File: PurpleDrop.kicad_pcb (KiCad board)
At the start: 4 copper layers, 161 x 92 mm, 156 parts, among them J1 Conn_02x32_Odd_Even, J10 current shunt, J2 Conn_02x32_Odd_Even, J3 Conn_02x20_Odd_Even, J4 Conn_01x04, J5 Conn_01x04, J6 Conn_01x04, J7 Conn_02x04_Odd_Even, J8 Conn_02x10_Odd_Even, J9 Barrel_Jack_Switch, Q1 SSM3K329R, Q2 SSM3K329R, Q3 SSM3K329R, Q4 SSM3K329R, SW1 SW_SPDT, U1 HV507, U10 TL7702B, U11 LR8N8-G, U2 HV507, U3 74LVC2T45DCT, U4 74LVC2T45DCT, U5 74LVC2T45DCT, U6 MAX31865AA, U7 MAX31865AA, U8 PCA9685PW, U9 MAX31865AA

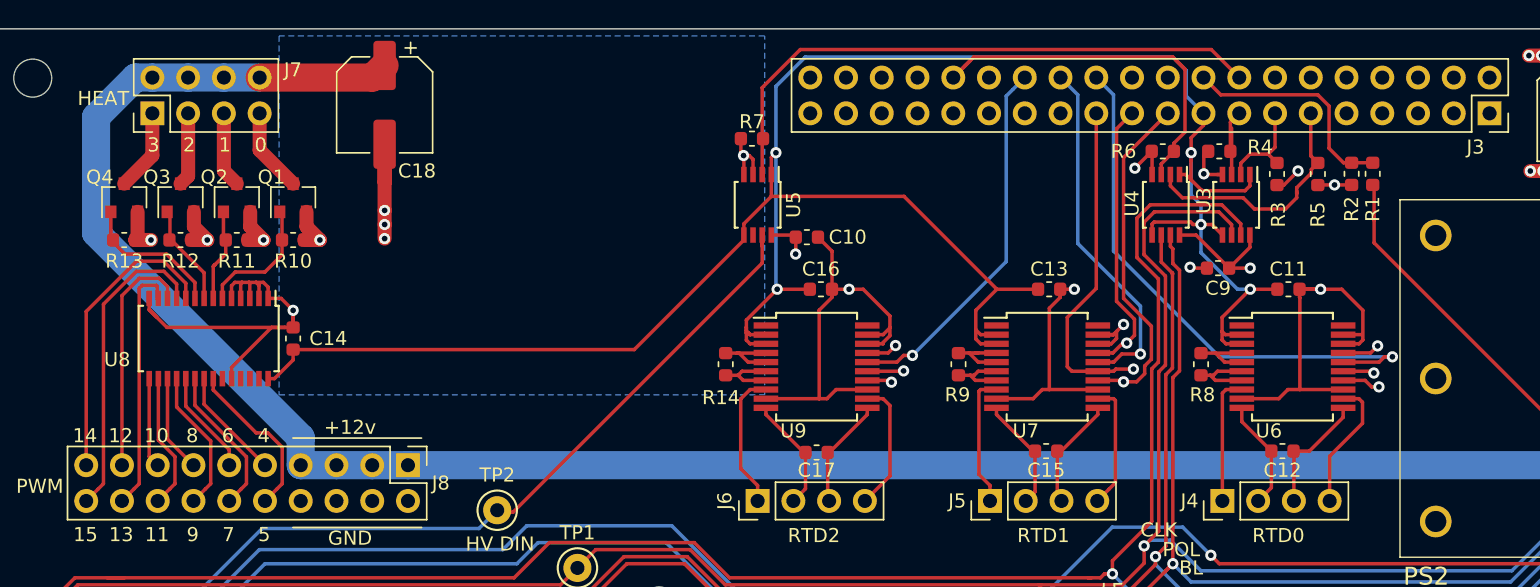
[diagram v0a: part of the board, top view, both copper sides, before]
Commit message: fixed missing i2c traces.  moved inner traces for SPI to back side
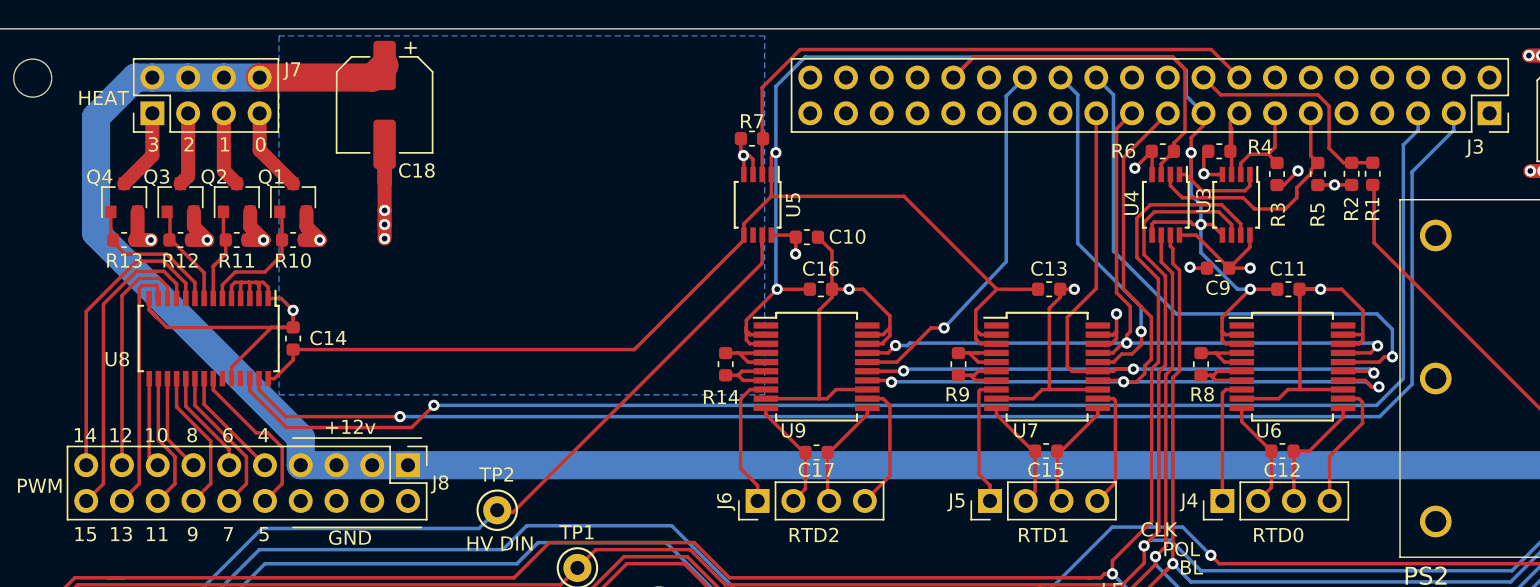
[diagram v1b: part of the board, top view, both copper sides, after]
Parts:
- renumbered He to H4
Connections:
- J3 pad 1: Net-(J3-Pad1) -> (no net)
- J3 pad 10: Net-(J3-Pad10) -> (no net)
- J3 pad 12: Net-(J3-Pad12) -> (no net)
- J3 pad 22: Net-(J3-Pad22) -> (no net)
- J3 pad 27: Net-(J3-Pad27) -> (no net)
- J3 pad 29: Net-(J3-Pad29) -> (no net)
- J3 pad 3: Net-(J3-Pad3) -> SDA
- J3 pad 31: Net-(J3-Pad31) -> (no net)
- J3 pad 33: Net-(J3-Pad33) -> (no net)
- J3 pad 35: Net-(J3-Pad35) -> (no net)
- J3 pad 36: Net-(J3-Pad36) -> (no net)
- J3 pad 37: Net-(J3-Pad37) -> (no net)
- J3 pad 38: Net-(J3-Pad38) -> (no net)
- J3 pad 40: Net-(J3-Pad40) -> (no net)
- J3 pad 5: Net-(J3-Pad5) -> SCL
- J3 pad 7: Net-(J3-Pad7) -> (no net)
- J3 pad 8: Net-(J3-Pad8) -> (no net)
- PS2 pad 1: Net-(PS2-Pad1) -> (no net)
- PS2 pad 5: Net-(PS2-Pad5) -> (no net)
- SW1 pad 1: Net-(SW1-Pad1) -> (no net)
- U1 pad 27: Net-(U1-Pad27) -> (no net)
- U1 pad 28: Net-(U1-Pad28) -> (no net)
- U1 pad 35: Net-(U1-Pad35) -> (no net)
- U1 pad 36: Net-(U1-Pad36) -> (no net)
- U2 pad 27: Net-(U2-Pad27) -> (no net)
- U2 pad 28: Net-(U2-Pad28) -> (no net)
- U2 pad 35: Net-(U2-Pad35) -> (no net)
- U2 pad 36: Net-(U2-Pad36) -> (no net)
- U5 pad 6: Net-(U5-Pad6) -> (no net)
- U6 pad 1: Net-(U6-Pad1) -> (no net)
- U7 pad 1: Net-(U7-Pad1) -> (no net)
- U8 pad 23: /peripherals/PWM_OE -> (no net)
- U8 pad 25: Net-(U8-Pad25) -> (no net)
- U8 pad 26: /peripherals/SCL -> SCL
- U8 pad 27: /peripherals/SDA -> SDA
- U9 pad 1: Net-(U9-Pad1) -> (no net)
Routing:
- net SDA: track 0.00 -> 104.9 mm, vias 0 -> 1
- net SCL: track 0.00 -> 104.6 mm, vias 0 -> 1
- net pi_CE0_0: track 39.4 -> 40.6 mm
- net GND: track 640.6 -> 641.2 mm
